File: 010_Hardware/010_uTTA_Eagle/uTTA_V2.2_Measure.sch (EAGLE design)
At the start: 286 parts, among them IC101.1 LT1167, IC101.2 LT1167, IC101.3 LT1167, IC101.4 LT1167, IC151.1 MCP602SN, IC151.3 MCP602SN, IC301 AD5664, IC302 LT1004CLP-2.5, IC303 TL074D, IC351.1 AD8672ARZ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

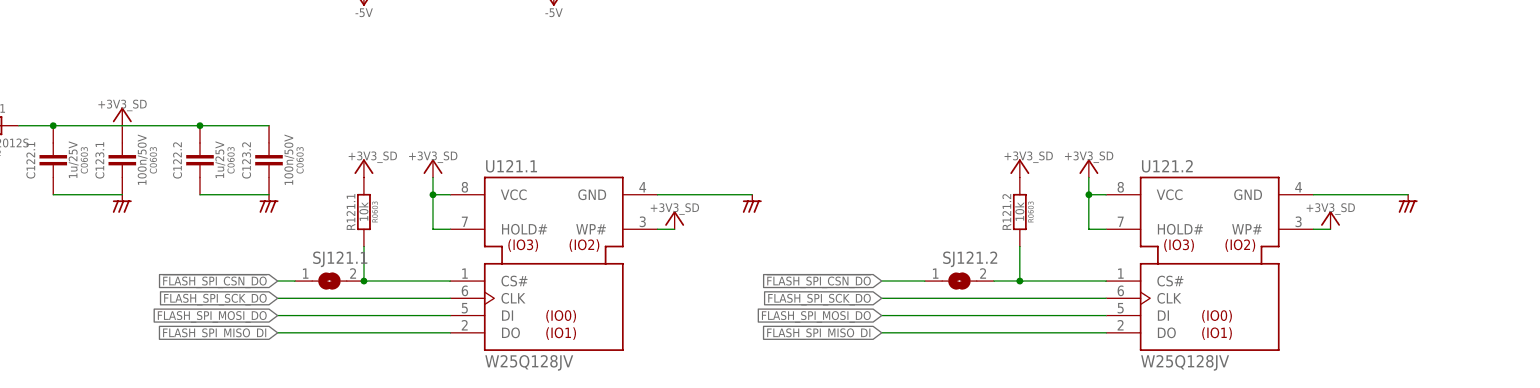
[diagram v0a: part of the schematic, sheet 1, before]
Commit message: Update to uTTA Version 2.2
Full update of both PCBs to HW Version 2.2:
Removed spare FLASH Memory
Adjusted Position of LEDs and Buttons
Cleanup of layout
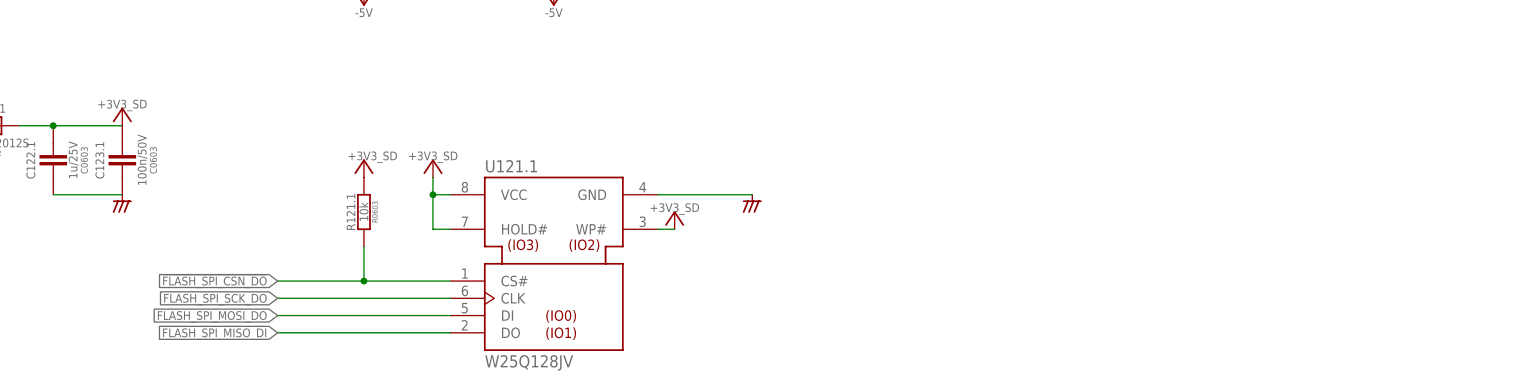
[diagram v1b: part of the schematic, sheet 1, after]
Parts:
- removed C122.2: 1u/25V, A_Kondensatoren:C-EUC0603
- removed C123.2: 100n/50V, A_Kondensatoren:C-EUC0603
- removed JP323: (no value), Connectors jumper:JP2E
- removed R121.2: 10k, A_Resistor:R-EU_R0603
- removed SJ121.1, SJ121.2: (no value), jumper:SJ
- removed U121.2: W25Q128JV, XMC4500_Relax-V1:W25Q80BVSSIG
- C107.1, C107.2, C107.3, C107.4: value 100n/50V -> DNP
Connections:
- removed net !FLASH1_SPI_CSN: R121.1.2, SJ121.1.2, U121.1.CS#
- removed net !FLASH2_SPI_CSN: R121.2.2, SJ121.2.2, U121.2.CS#
- net !FLASH_SPI_CSN_DO: now also R121.1.2, U121.1.CS#; no longer SJ121.1.1, SJ121.2.1
- net +5V/4: no longer C122.2.1, C123.2.1, R121.2.1, U121.2.HOLD#, U121.2.VCC, U121.2.WP#
- net AGND: no longer C122.2.2, C123.2.2, JP323.2, U121.2.GND
- net FLASH_SPI_MISO_DI: no longer U121.2.DO
- net FLASH_SPI_MOSI_DO: no longer U121.2.DI
- net FLASH_SPI_SCK_DO: no longer U121.2.CLK
- net V_OFF0: no longer JP323.1
- net V_OFF1_3: no longer JP323.3
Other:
- note added: "V_OFF1 = ~-1.24V...2.5V Step Width = ~57.07µV"
- note removed: "Testpoint for Offset Voltage Calibration"
- moved on the sheet: C152.1, IC151.1P

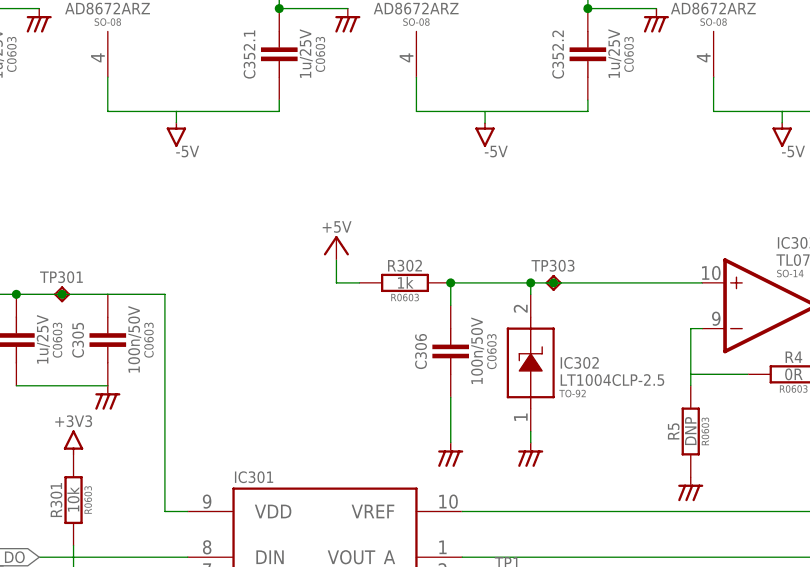
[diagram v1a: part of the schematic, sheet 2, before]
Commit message: removed outdated variants from design
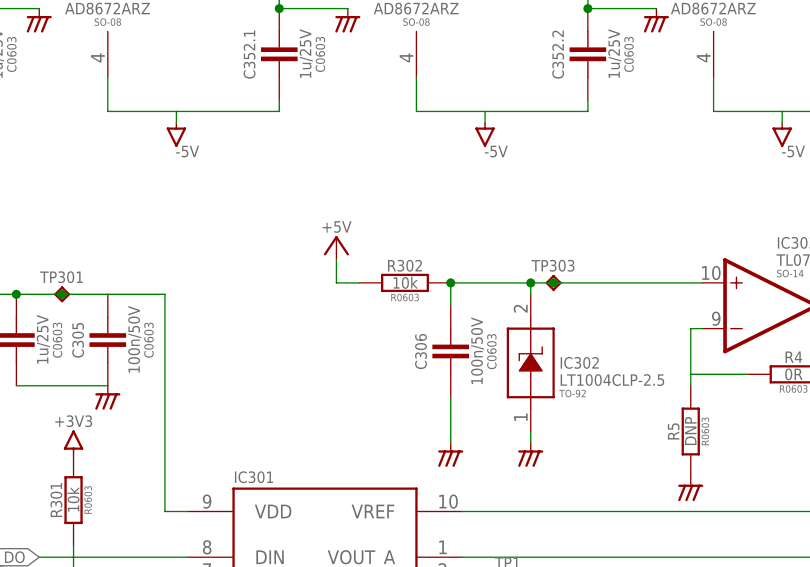
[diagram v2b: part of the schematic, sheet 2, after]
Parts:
- R302: value 1k -> 10k
